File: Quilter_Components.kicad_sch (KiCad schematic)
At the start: 38 parts, among them J1 Conn_01x10_Male, J2 Conn_01x10_Male, J3 Conn_01x10_Male, J4 Eurorack_10_pin_power, U1 TL072, U2 TL074, U3 TL074, U4 TL074

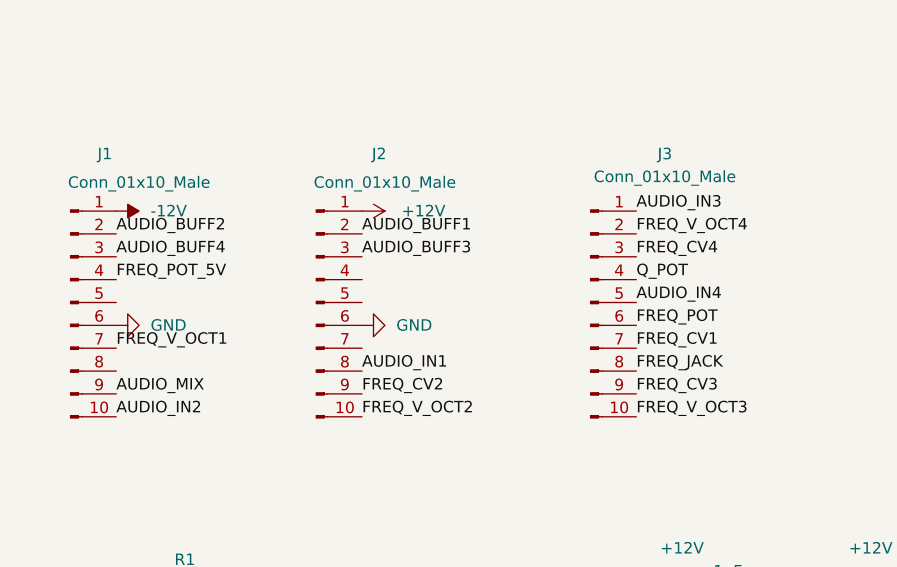
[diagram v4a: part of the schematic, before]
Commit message: Finished routing components and controls
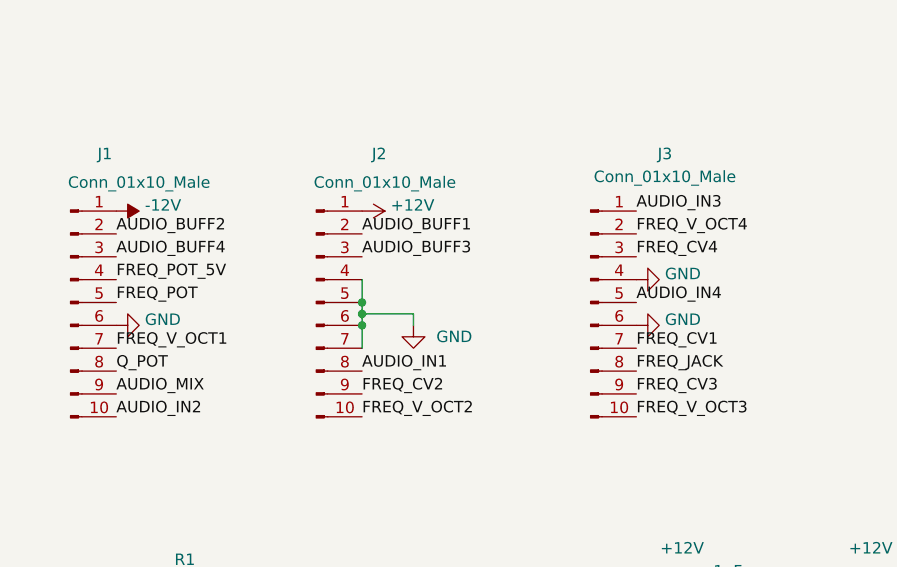
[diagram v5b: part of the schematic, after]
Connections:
- net FREQ_POT: now also J1.5 (Pin_5); no longer J3.6 (Pin_6)
- net GND: now also J2.4 (Pin_4), J2.5 (Pin_5), J2.7 (Pin_7), J3.4 (Pin_4), J3.6 (Pin_6)
- net Q_POT: now also J1.8 (Pin_8); no longer J3.4 (Pin_4)
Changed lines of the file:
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@@
   (junction (at 113.03 148.59) (diameter 0) (color 0 0 0 0)
   )
+  (junction (at 56.515 98.425) (diameter 0) (color 0 0 0 0)
+  )
   (junction (at 239.395 60.325) (diameter 1.016) (color 0 0 0 0)
   )
@@
   (junction (at 257.175 93.345) (diameter 1.016) (color 0 0 0 0)
   )
+  (junction (at 56.515 99.695) (diameter 0) (color 0 0 0 0)
+  )
   (junction (at 36.195 169.545) (diameter 0) (color 0 0 0 0)
   )
@@
   (junction (at 24.765 172.085) (diameter 0) (color 0 0 0 0)
   )
+  (junction (at 56.515 100.965) (diameter 0) (color 0 0 0 0)
+  )
   (junction (at 48.895 167.005) (diameter 0) (color 0 0 0 0)
   )
@@
     (stroke (width 0) (type solid) (color 0 0 0 0))
   )
+  (wire (pts (xy 62.23 100.965) (xy 62.23 99.695))
+    (stroke (width 0) (type default) (color 0 0 0 0))
+  )
   (wire (pts (xy 174.625 99.695) (xy 174.625 103.505))
     (stroke (width 0) (type solid) (color 0 0 0 0))
@@
     (stroke (width 0) (type default) (color 0 0 0 0))
   )
+  (wire (pts (xy 62.23 99.695) (xy 56.515 99.695))
+    (stroke (width 0) (type default) (color 0 0 0 0))
+  )
   (wire (pts (xy 24.765 172.085) (xy 24.765 183.515))
     (stroke (width 0) (type default) (color 0 0 0 0))
@@
     (stroke (width 0) (type solid) (color 0 0 0 0))
   )
+  (wire (pts (xy 56.515 99.695) (xy 56.515 100.965))
+    (stroke (width 0) (type default) (color 0 0 0 0))
+  )
   (wire (pts (xy 239.395 83.185) (xy 245.745 83.185))
     (stroke (width 0) (type solid) (color 0 0 0 0))
@@
     (stroke (width 0) (type solid) (color 0 0 0 0))
   )
+  (wire (pts (xy 56.515 95.885) (xy 56.515 98.425))
+    (stroke (width 0) (type default) (color 0 0 0 0))
+  )
   (wire (pts (xy 148.59 34.29) (xy 151.13 34.29))
     (stroke (width 0) (type default) (color 0 0 0 0))
@@
     (stroke (width 0) (type solid) (color 0 0 0 0))
   )
+  (wire (pts (xy 56.515 100.965) (xy 56.515 103.505))
+    (stroke (width 0) (type default) (color 0 0 0 0))
+  )
   (wire (pts (xy 176.53 138.43) (xy 175.26 138.43))
     (stroke (width 0) (type default) (color 0 0 0 0))
@@
     (stroke (width 0) (type default) (color 0 0 0 0))
   )
+  (wire (pts (xy 56.515 98.425) (xy 56.515 99.695))
+    (stroke (width 0) (type default) (color 0 0 0 0))
+  )
   (wire (pts (xy 239.395 121.285) (xy 240.665 121.285))
     (stroke (width 0) (type solid) (color 0 0 0 0))
@@
     (effects (font (size 1.27 1.27)) (justify right bottom))
   )
-  (label "Q_POT" (at 86.995 95.885 0)
+  (label "Q_POT" (at 29.21 106.045 0)
     (effects (font (size 1.27 1.27)) (justify left bottom))
   )
@@
     (effects (font (size 1.27 1.27)) (justify left bottom))
   )
-  (label "FREQ_POT" (at 86.995 100.965 0)
+  (label "FREQ_POT" (at 29.21 98.425 0)
     (effects (font (size 1.27 1.27)) (justify left bottom))
   )
@@
     (pin "1")
     (pin "2")
+  )
+  (symbol (lib_id "power:GND") (at 86.995 95.885 90) (unit 1)
+    (in_bom yes) (on_board yes)
+    (property "Reference" "#PWR?" (id 0) (at 93.345 95.885 0)
+      (effects (font (size 1.27 1.27)) hide)
+    )
+    (property "Value" "GND" (id 1) (at 90.17 95.25 90)
+      (effects (font (size 1.27 1.27)) (justify right))
+    )
+    (property "Footprint" "" (id 2) (at 86.995 95.885 0)
+      (effects (font (size 1.27 1.27)) hide)
+    )
+    (property "Datasheet" "" (id 3) (at 86.995 95.885 0)
+      (effects (font (size 1.27 1.27)) hide)
+    )
+    (pin "1")
   )
   (symbol (lib_id "Amplifier_Operational:TL074") (at 89.535 176.53 0) (mirror y) (unit 5)
@@
   )
   (symbol (lib_id "power:+12V") (at 56.515 88.265 270) (unit 1)
-    (in_bom yes) (on_board yes) (fields_autoplaced)
+    (in_bom yes) (on_board yes)
     (property "Reference" "#PWR0110" (id 0) (at 52.705 88.265 0)
       (effects (font (size 1.27 1.27)) hide)
     )
-    (property "Value" "+12V" (id 1) (at 60.9143 88.2649 90)
+    (property "Value" "+12V" (id 1) (at 59.69 87.63 90)
       (effects (font (size 1.27 1.27)) (justify left))
     )
@@
   )
   (symbol (lib_id "power:-12V") (at 29.21 88.265 270) (unit 1)
-    (in_bom yes) (on_board yes) (fields_autoplaced)
+    (in_bom yes) (on_board yes)
     (property "Reference" "#PWR0109" (id 0) (at 31.75 88.265 0)
       (effects (font (size 1.27 1.27)) hide)
     )
-    (property "Value" "-12V" (id 1) (at 33.02 88.2649 90)
+    (property "Value" "-12V" (id 1) (at 32.385 87.63 90)
       (effects (font (size 1.27 1.27)) (justify left))
     )
@@
     (pin "4")
   )
+  (symbol (lib_id "power:GND") (at 86.995 100.965 90) (unit 1)
+    (in_bom yes) (on_board yes)
+    (property "Reference" "#PWR?" (id 0) (at 93.345 100.965 0)
+      (effects (font (size 1.27 1.27)) hide)
+    )
+    (property "Value" "GND" (id 1) (at 90.17 100.33 90)
+      (effects (font (size 1.27 1.27)) (justify right))
+    )
+    (property "Footprint" "" (id 2) (at 86.995 100.965 0)
+      (effects (font (size 1.27 1.27)) hide)
+    )
+    (property "Datasheet" "" (id 3) (at 86.995 100.965 0)
+      (effects (font (size 1.27 1.27)) hide)
+    )
+    (pin "1")
+  )
   (symbol (lib_id "Device:R_Small") (at 170.815 103.505 270) (unit 1)
     (in_bom yes) (on_board yes)
@@
     (pin "1")
   )
-  (symbol (lib_id "power:GND") (at 56.515 100.965 90) (unit 1)
-    (in_bom yes) (on_board yes) (fields_autoplaced)
-    (property "Reference" "#PWR06" (id 0) (at 62.865 100.965 0)
-      (effects (font (size 1.27 1.27)) hide)
-    )
-    (property "Value" "GND" (id 1) (at 60.325 100.9649 90)
-      (effects (font (size 1.27 1.27)) (justify right))
-    )
-    (property "Footprint" "" (id 2) (at 56.515 100.965 0)
-      (effects (font (size 1.27 1.27)) hide)
-    )
-    (property "Datasheet" "" (id 3) (at 56.515 100.965 0)
-      (effects (font (size 1.27 1.27)) hide)
-    )
-    (pin "1")
-  )
   (symbol (lib_id "Device:R_Small") (at 235.585 90.805 270) (unit 1)
     (in_bom yes) (on_board yes)
@@
     (pin "1")
   )
+  (symbol (lib_id "power:GND") (at 62.23 100.965 0) (unit 1)
+    (in_bom yes) (on_board yes) (fields_autoplaced)
+    (property "Reference" "#PWR?" (id 0) (at 62.23 107.315 0)
+      (effects (font (size 1.27 1.27)) hide)
+    )
+    (property "Value" "GND" (id 1) (at 64.77 102.2349 0)
+      (effects (font (size 1.27 1.27)) (justify left))
+    )
+    (property "Footprint" "" (id 2) (at 62.23 100.965 0)
+      (effects (font (size 1.27 1.27)) hide)
+    )
+    (property "Datasheet" "" (id 3) (at 62.23 100.965 0)
+      (effects (font (size 1.27 1.27)) hide)
+    )
+    (pin "1")
+  )
   (symbol (lib_id "power:GND") (at 102.235 170.18 0) (unit 1)
     (in_bom yes) (on_board yes)
@@
       (effects (font (size 1.27 1.27)) hide)
     )
-    (property "Value" "GND" (id 1) (at 33.02 100.9649 90)
+    (property "Value" "GND" (id 1) (at 32.385 100.33 90)
       (effects (font (size 1.27 1.27)) (justify right))
     )
@@
       (reference "#PWR05") (unit 1) (value "GND") (footprint "")
     )
-    (path "/62dc216a-4642-4a51-b11b-bb1a3484fa96"
-      (reference "#PWR06") (unit 1) (value "GND") (footprint "")
-    )
     (path "/ae95714b-7be4-4c70-9dbd-e5eeedd53a0e"
       (reference "#PWR07") (unit 1) (value "+12V") (footprint "")
@@
       (reference "#PWR0110") (unit 1) (value "+12V") (footprint "")
     )
+    (path "/09a5e742-458d-4e9b-aa99-269ec9aa302b"
+      (reference "#PWR?") (unit 1) (value "GND") (footprint "")
+    )
+    (path "/311e63e2-55b1-49d2-9d74-809bca2e65b5"
+      (reference "#PWR?") (unit 1) (value "GND") (footprint "")
+    )
+    (path "/91cd4b2c-aa96-4319-aa6a-a0ba1deab567"
+      (reference "#PWR?") (unit 1) (value "GND") (footprint "")
+    )
     (path "/2c333ca4-0780-4b24-87eb-2f414d90e6bb"

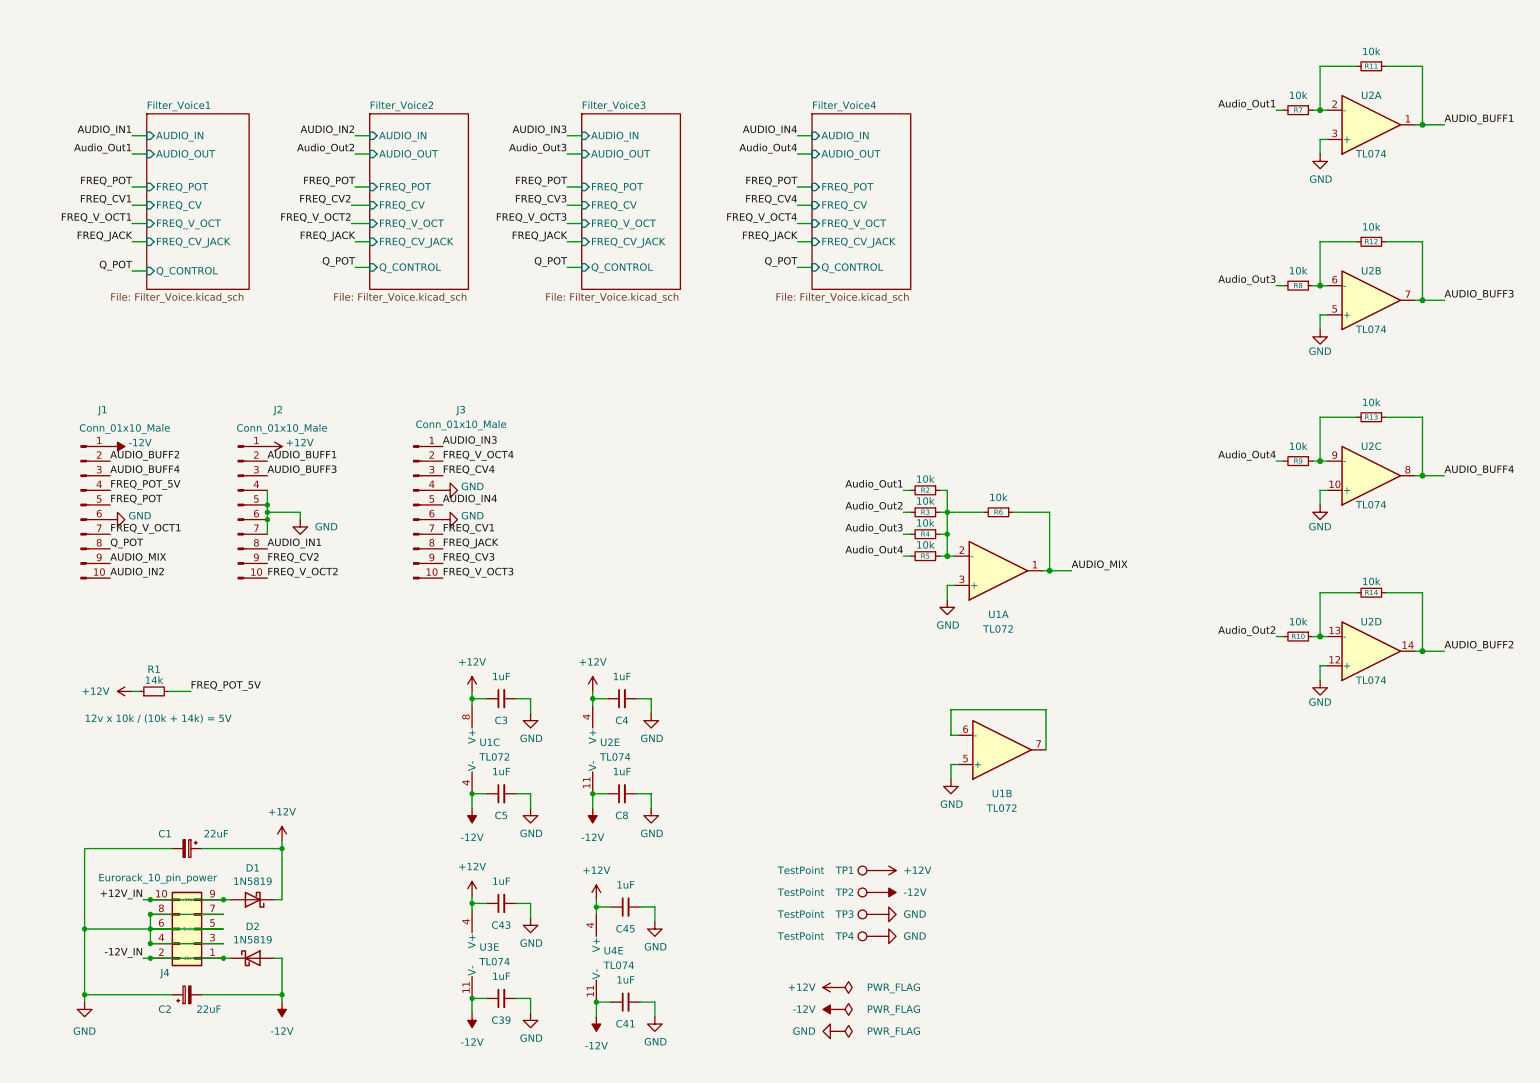
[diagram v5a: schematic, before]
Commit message: Schematic formatting
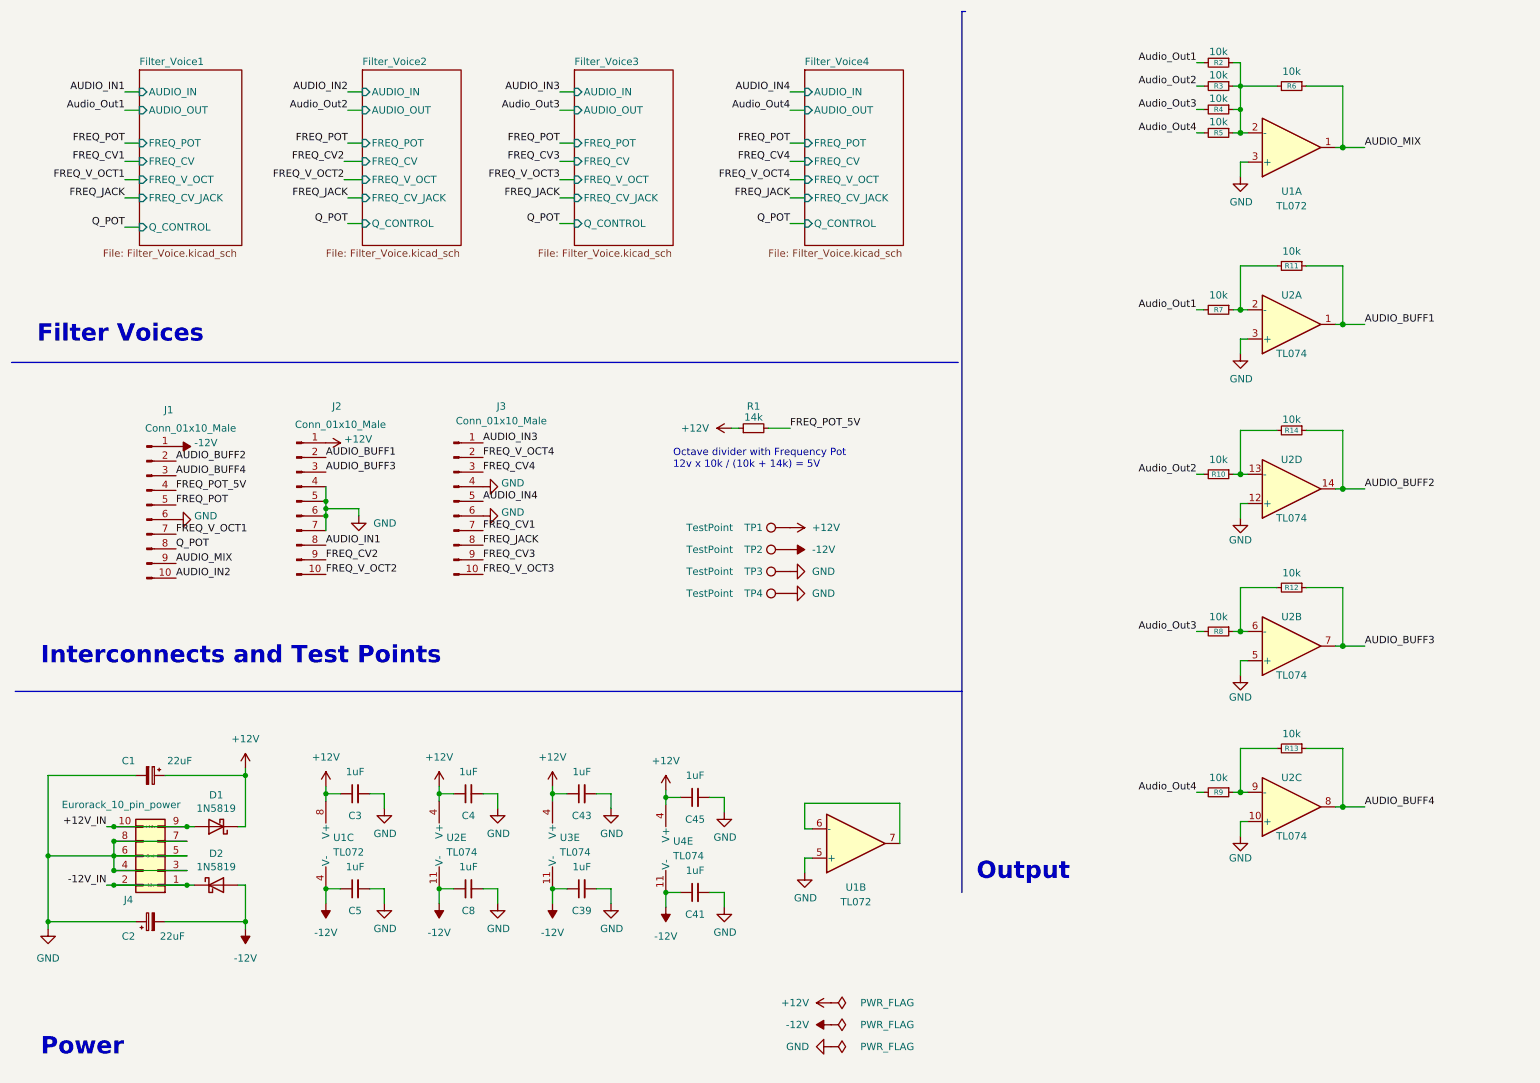
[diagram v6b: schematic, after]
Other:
- note added: "Filter Voices"
- note added: "Interconnects and Test Points"
- note added: "Octave divider with Frequency Pot 12v x 10k / (10k + 14k) = 5V"
- note added: "Output"
- note added: "Power"
- note removed: "12v x 10k / (10k + 14k) = 5V"
- moved on the sheet: C1, C2, C3, C39, C4, C41, C43, C45, C5, C8, D1, D2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

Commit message: Cleaned up panel and PCBs
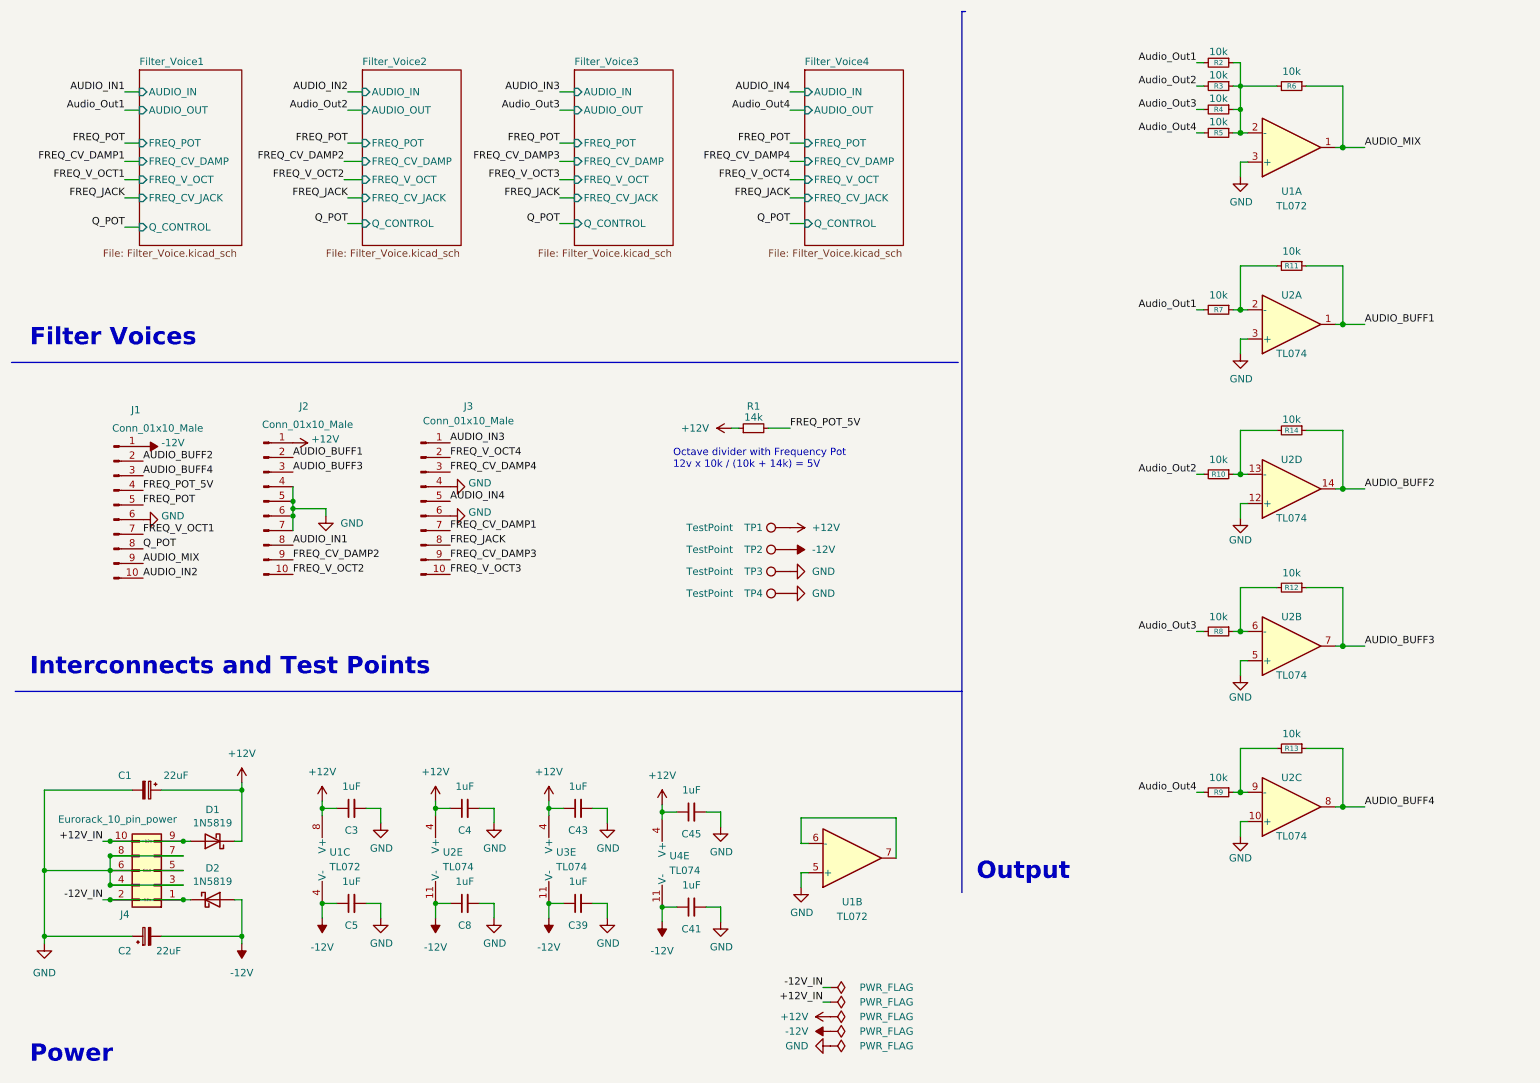
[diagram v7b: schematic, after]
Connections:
- net FREQ_CV1 renamed FREQ_CV_DAMP1
- net FREQ_CV2 renamed FREQ_CV_DAMP2
- net FREQ_CV3 renamed FREQ_CV_DAMP3
- net FREQ_CV4 renamed FREQ_CV_DAMP4
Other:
- sheet Filter_Voice1 ports: added FREQ_CV_DAMP; removed FREQ_CV
- sheet Filter_Voice2 ports: added FREQ_CV_DAMP; removed FREQ_CV
- sheet Filter_Voice3 ports: added FREQ_CV_DAMP; removed FREQ_CV
- sheet Filter_Voice4 ports: added FREQ_CV_DAMP; removed FREQ_CV
- moved on the sheet: C1, C2, C3, C39, C4, C41, C43, C45, C5, C8, D1, D2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
